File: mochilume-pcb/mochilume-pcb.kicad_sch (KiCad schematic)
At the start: 16 parts

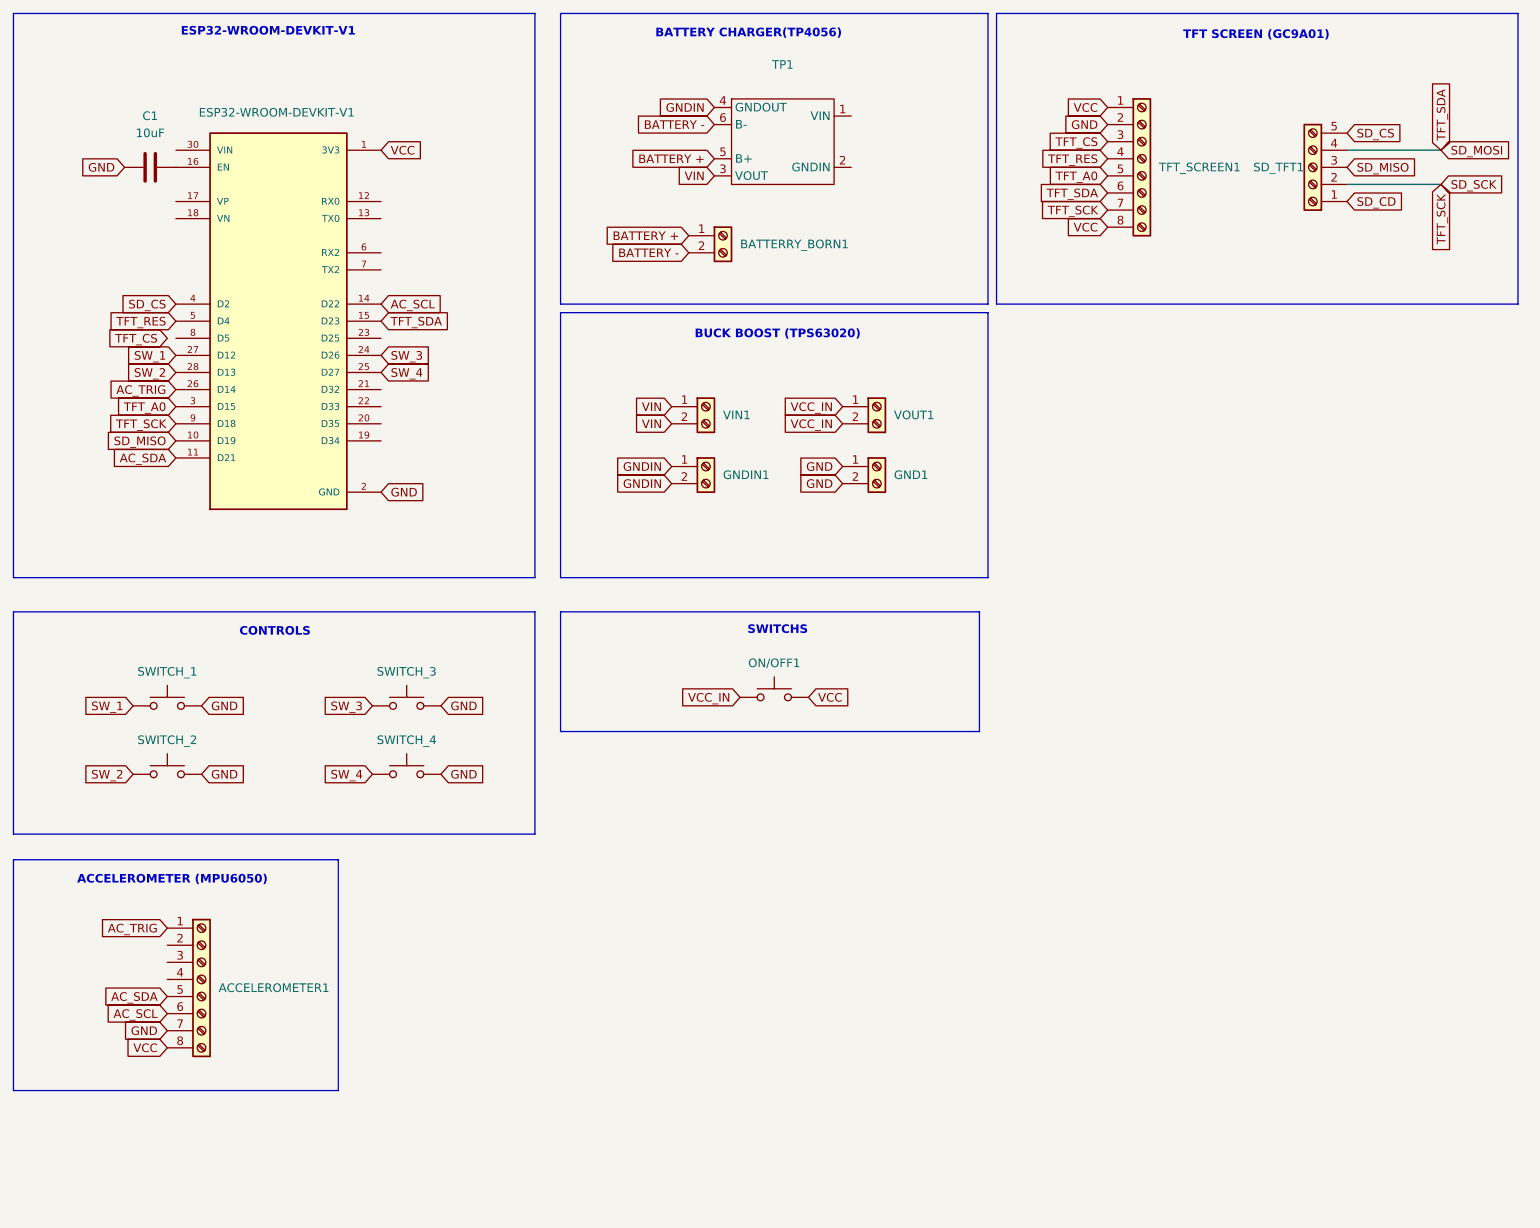
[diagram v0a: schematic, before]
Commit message: update pcb: remove sd card tracks
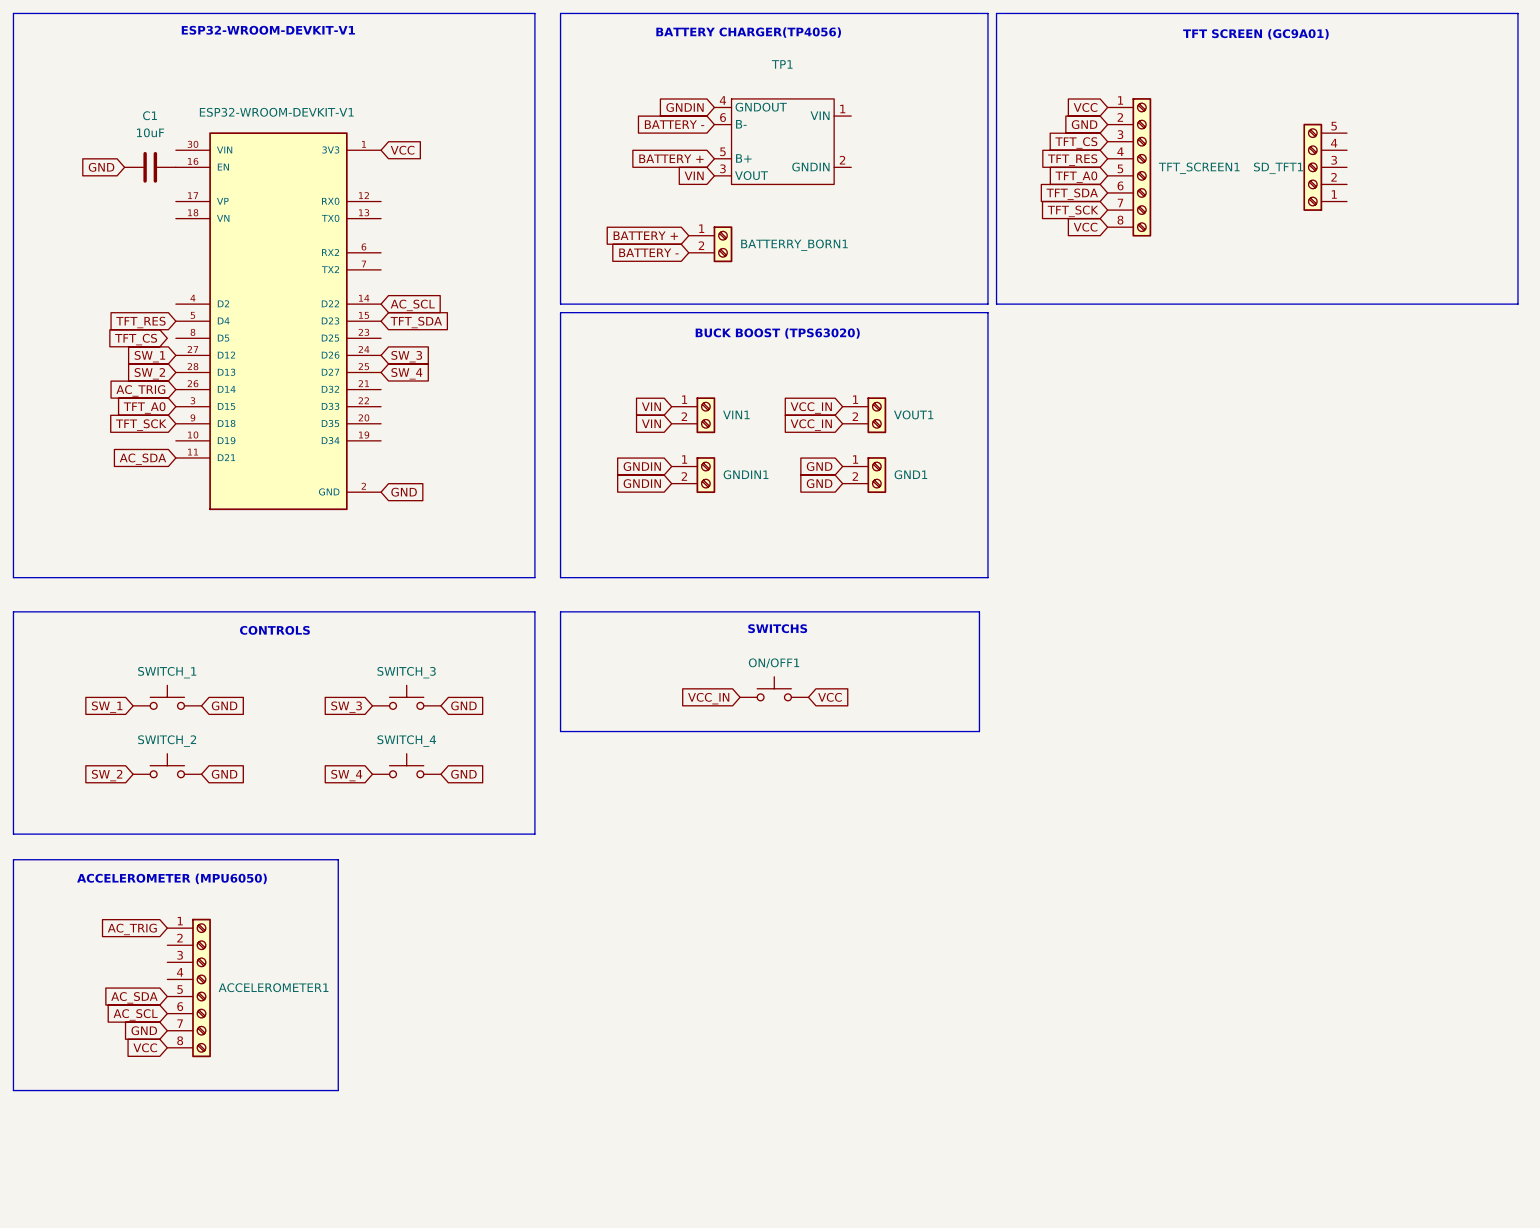
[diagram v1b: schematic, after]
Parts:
- ACCELEROMETER1, BATTERRY_BORN1, ESP32-WROOM-DEVKIT-V1, GND1, GNDIN1, ON/OFF1, SD_TFT1, SWITCH_1, SWITCH_2, SWITCH_3, SWITCH_4, TFT_SCREEN1, TP1, VIN1, VOUT1: value ~ -> (none)
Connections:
- net SD_CD: no longer names the net of SD_TFT1.1 (Pin_1)
- net SD_CS: no longer names the net of ESP32-WROOM-DEVKIT-V1.4 (D2)
- net SD_CS: no longer SD_TFT1.5 (Pin_5)
- net SD_MISO: no longer names the net of ESP32-WROOM-DEVKIT-V1.10 (D19)
- net SD_MISO: no longer SD_TFT1.3 (Pin_3)
- net SD_MOSI renamed TFT_SDA
- net TFT_SDA: no longer SD_TFT1.4 (Pin_4)
- net SD_SCK renamed TFT_SCK
- net TFT_SCK: no longer SD_TFT1.2 (Pin_2)

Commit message: feat pcb: add lora module and 2 buttons to kicad schematic
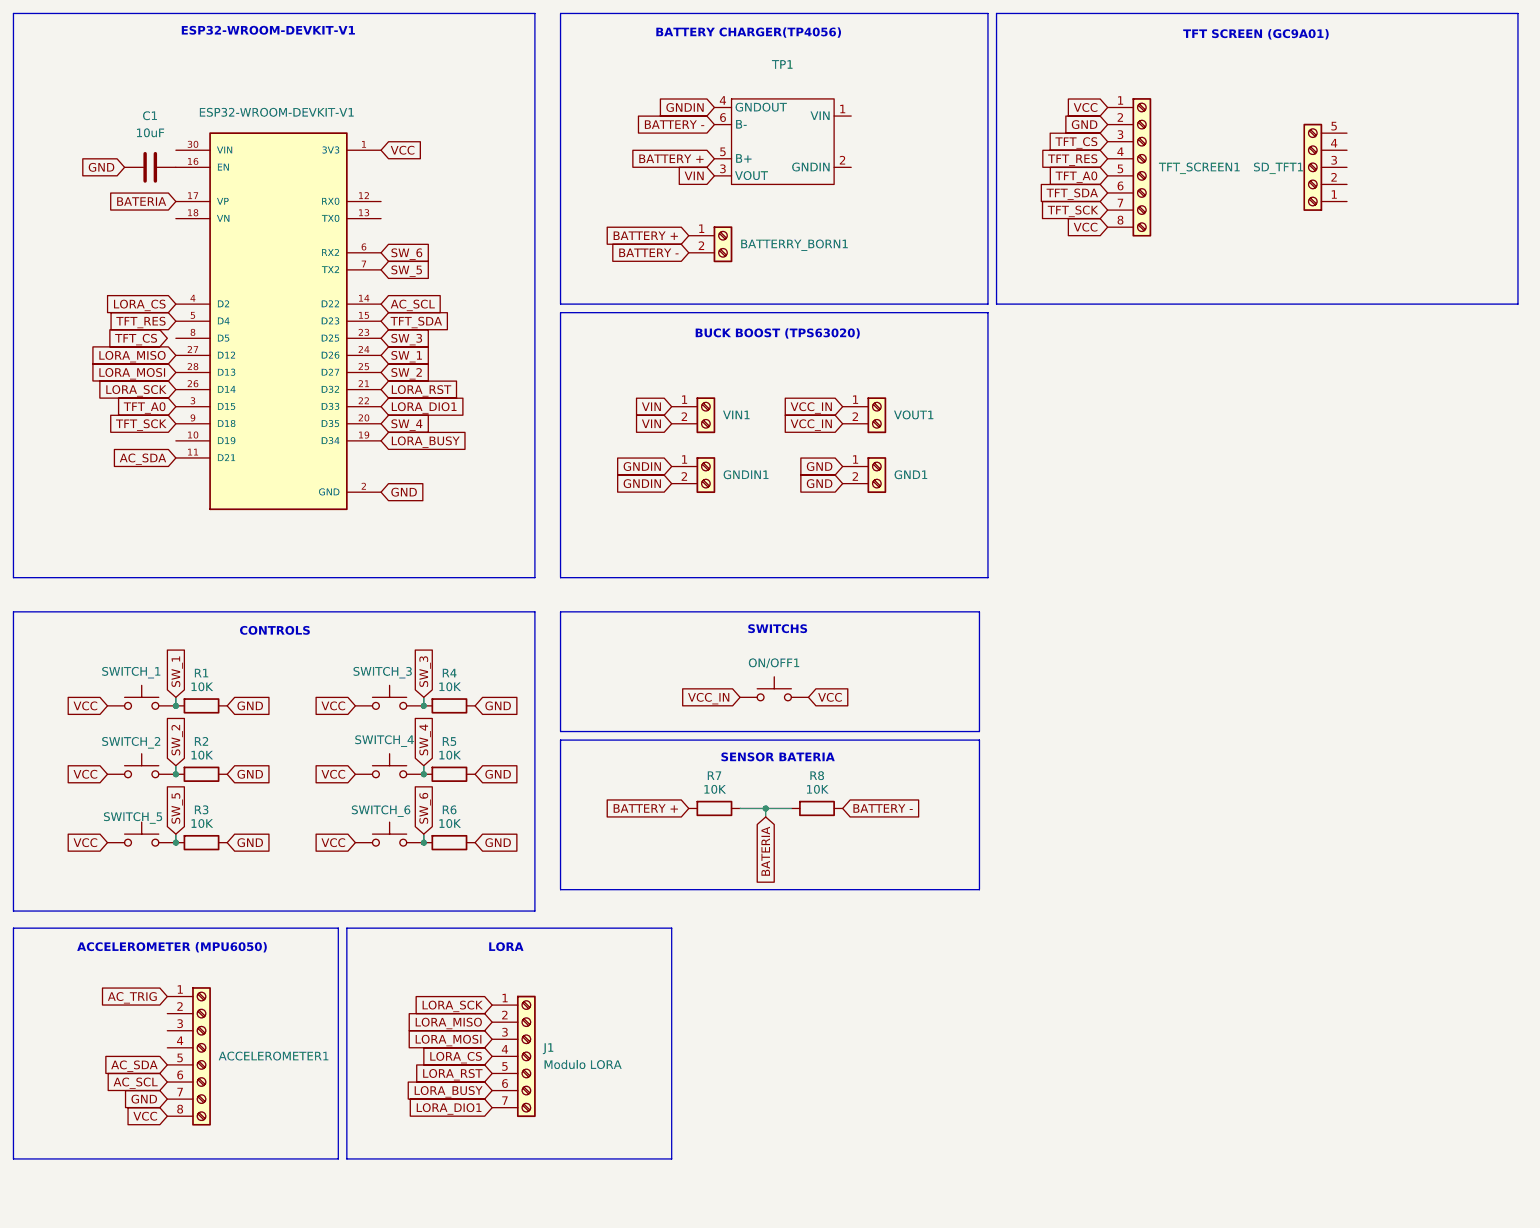
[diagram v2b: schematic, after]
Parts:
- added J1: Modulo LORA, symbol Connector:Screw_Terminal_01x07
- added R1, R2, R3, R4, R5, R6, R7, R8: 10K, symbol Device:R
- added SWITCH_5, SWITCH_6: (no value), Button_Switch_THT:SW_PUSH_6mm, symbol Switch:SW_Push
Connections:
- net AC_TRIG: no longer ESP32-WROOM-DEVKIT-V1.26 (D14)
- net BATTERY +: now also R7.2
- net BATTERY -: now also R8.1
- net GND: now also R1.1, R2.1, R3.1, R4.1, R5.1, R6.1; no longer SWITCH_1.2, SWITCH_2.2, SWITCH_3.2, SWITCH_4.2
- net SW_1: now also ESP32-WROOM-DEVKIT-V1.24 (D26), SWITCH_1.2, R1.2; no longer ESP32-WROOM-DEVKIT-V1.27 (D12), SWITCH_1.1
- net SW_2: now also ESP32-WROOM-DEVKIT-V1.25 (D27), SWITCH_2.2, R2.2; no longer ESP32-WROOM-DEVKIT-V1.28 (D13), SWITCH_2.1
- net SW_3: now also ESP32-WROOM-DEVKIT-V1.23 (D25), SWITCH_3.2, R4.2; no longer ESP32-WROOM-DEVKIT-V1.24 (D26), SWITCH_3.1
- net SW_4: now also ESP32-WROOM-DEVKIT-V1.20 (D35), SWITCH_4.2, R5.2; no longer ESP32-WROOM-DEVKIT-V1.25 (D27), SWITCH_4.1
- net VCC: now also SWITCH_1.1, SWITCH_2.1, SWITCH_3.1, SWITCH_4.1, SWITCH_5.1, SWITCH_6.1
- net BATERIA: now reaches ESP32-WROOM-DEVKIT-V1.17 (VP)
- net BATERIA: now also R7.1, R8.2
- net LORA_BUSY: now reaches ESP32-WROOM-DEVKIT-V1.19 (D34)
- net LORA_BUSY: now also J1.6 (Pin_6)
- net LORA_RST: now reaches ESP32-WROOM-DEVKIT-V1.21 (D32)
- net LORA_RST: now also J1.5 (Pin_5)
- net LORA_DIO1: now reaches ESP32-WROOM-DEVKIT-V1.22 (D33)
- net LORA_DIO1: now also J1.7 (Pin_7)
- net LORA_CS: now reaches ESP32-WROOM-DEVKIT-V1.4 (D2)
- net LORA_CS: now also J1.4 (Pin_4)
- net SW_6: now reaches ESP32-WROOM-DEVKIT-V1.6 (RX2)
- net SW_6: now also R6.2, SWITCH_6.2
- net SW_5: now reaches ESP32-WROOM-DEVKIT-V1.7 (TX2)
- net SW_5: now also R3.2, SWITCH_5.2
- new net LORA_MISO: ESP32-WROOM-DEVKIT-V1.27 (D12), J1.2 (Pin_2)
- new net LORA_MOSI: ESP32-WROOM-DEVKIT-V1.28 (D13), J1.3 (Pin_3)
- new net LORA_SCK: ESP32-WROOM-DEVKIT-V1.26 (D14), J1.1 (Pin_1)
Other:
- note added: "LORA"
- note added: "SENSOR BATERIA"
- moved on the sheet: ACCELEROMETER1, SWITCH_1, SWITCH_2, SWITCH_3, SWITCH_4

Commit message: fix pcb: fix schematics bugs
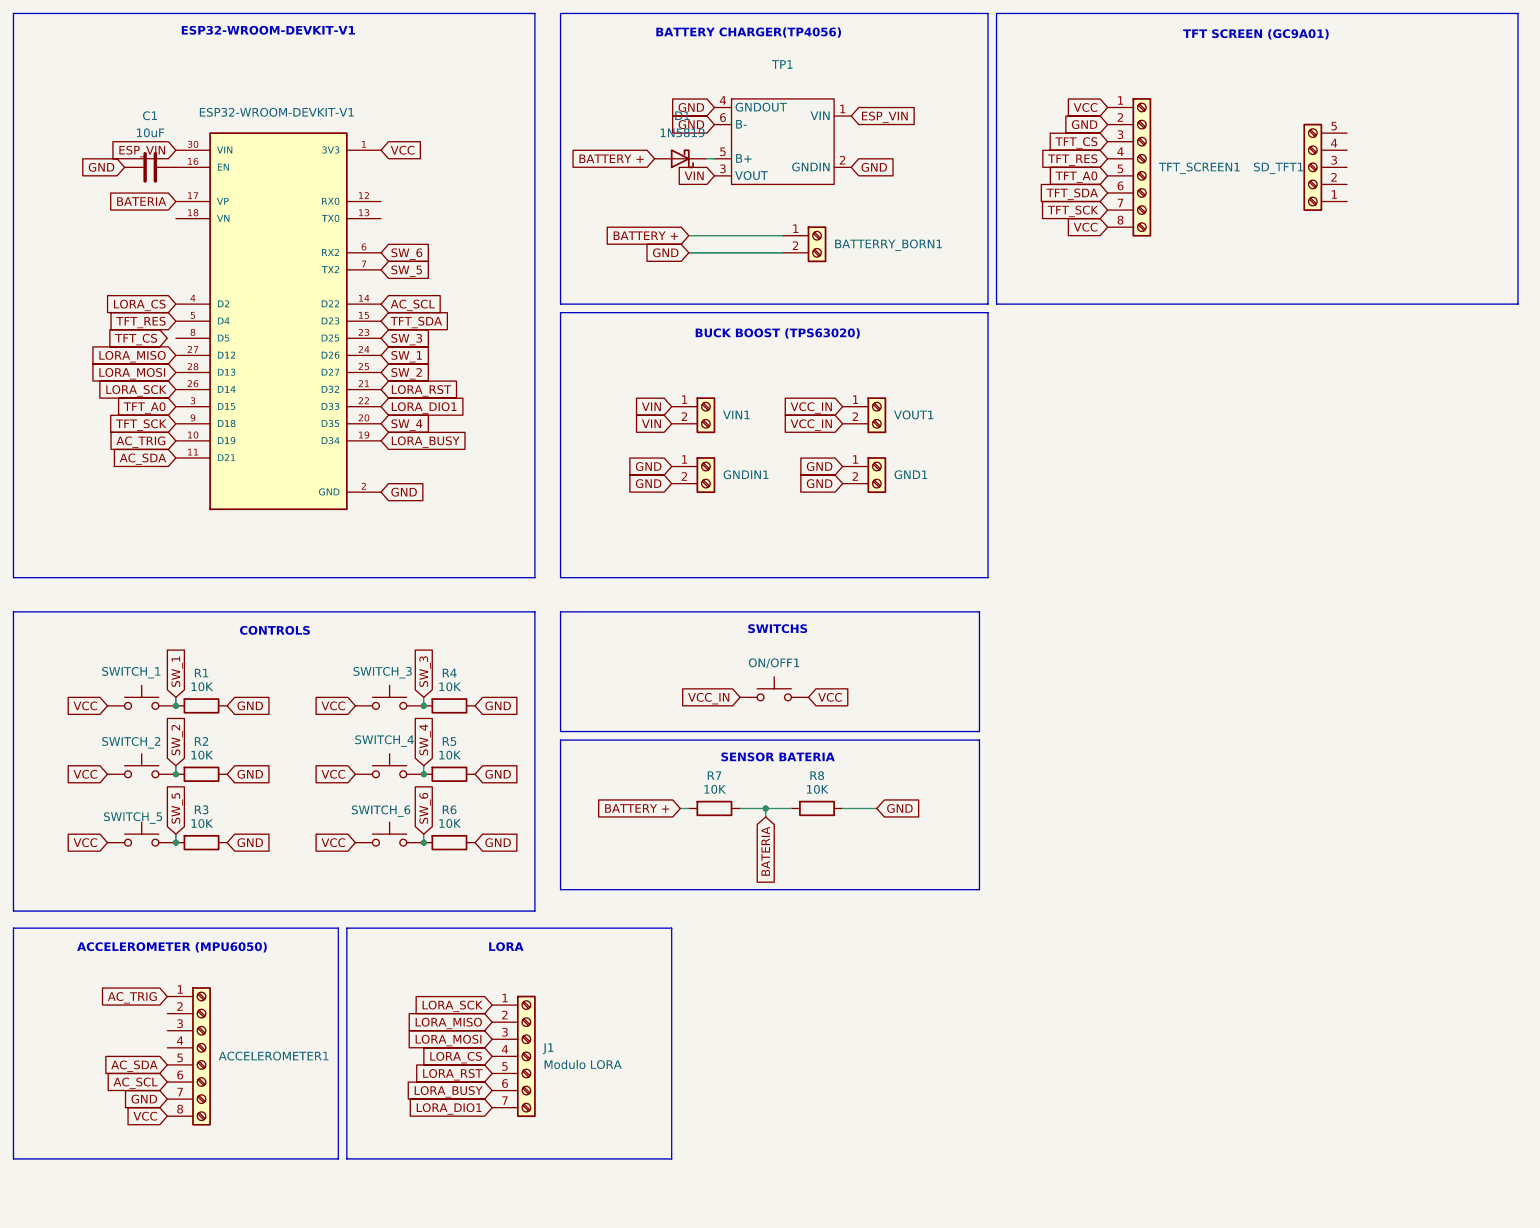
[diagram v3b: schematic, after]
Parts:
- added D1: 1N5819, Diode_THT:D_DO-41_SOD81_P10.16mm_Horizontal, symbol Diode:1N5819
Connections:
- net BATTERY - is gone; now on net GND: BATTERRY_BORN1.2 (Pin_2), R8.1, TP1.6 (B-)
- net GNDIN is gone; now on net GND: GNDIN1.1 (Pin_1), GNDIN1.2 (Pin_2), TP1.4 (GNDOUT)
- net AC_TRIG: now also ESP32-WROOM-DEVKIT-V1.10 (D19)
- net BATTERY +: now also D1.2 (A); no longer TP1.5 (B+)
- net GND: now also TP1.2 (GNDIN)
- net ESP_VIN: now reaches TP1.1 (VIN)
- net ESP_VIN: now also ESP32-WROOM-DEVKIT-V1.30 (VIN)
- new net: D1.1 (K), TP1.5 (B+)
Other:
- moved on the sheet: BATTERRY_BORN1

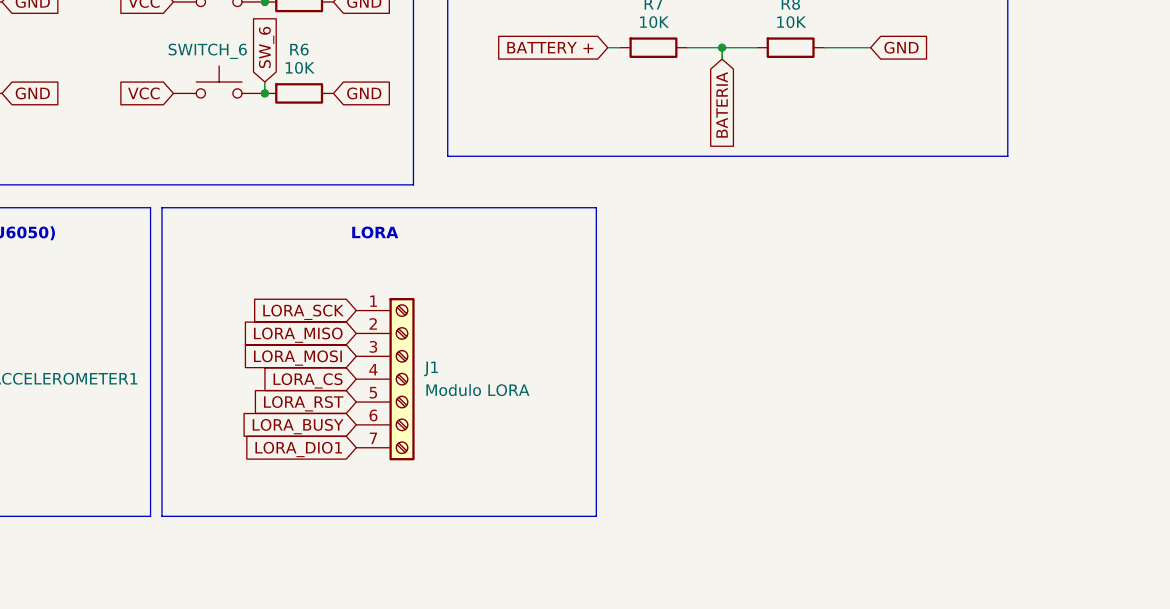
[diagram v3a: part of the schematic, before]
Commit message: fix pcb: update footprints and add pcb sketch without vias
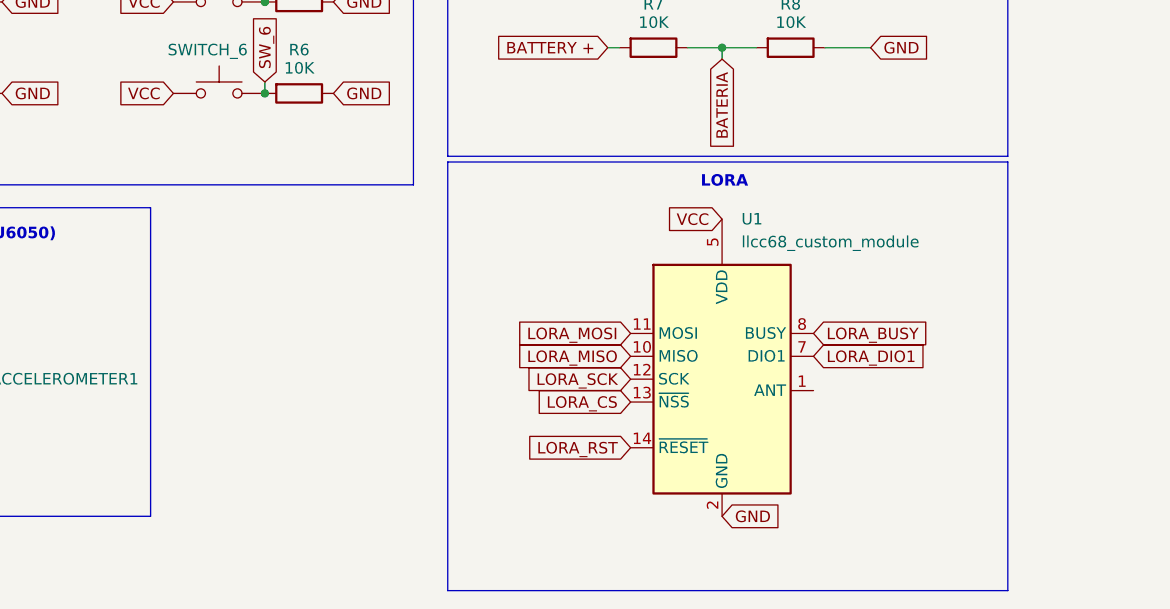
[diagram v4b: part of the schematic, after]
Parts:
- removed J1: Modulo LORA, symbol Connector:Screw_Terminal_01x07
- added U1: llcc68_custom_module, RF_Module:Ai-Thinker-Ra-01-LoRa, symbol custom:llcc68_custom_module
- R1, R2, R3, R4, R5, R6, R7, R8: footprint (none) -> Resistor_THT:R_Axial_DIN0309_L9.0mm_D3.2mm_P15.24mm_Horizontal
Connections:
- net GND: now also U1.16 (GND), U1.2 (GND), U1.9 (GND)
- net LORA_BUSY: now also U1.8 (BUSY)
- net LORA_CS: now also U1.13 (~{NSS})
- net LORA_DIO1: now also U1.7 (DIO1)
- net LORA_MISO: now also U1.10 (MISO)
- net LORA_MOSI: now also U1.11 (MOSI)
- net LORA_RST: now also U1.14 (~{RESET})
- net LORA_SCK: now also U1.12 (SCK)
- net VCC: now also U1.5 (VDD)
